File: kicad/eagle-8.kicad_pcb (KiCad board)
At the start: 4 copper layers, 127.1 x 96.7 mm, 33 parts, among them J1 SC242, J2 PGA387

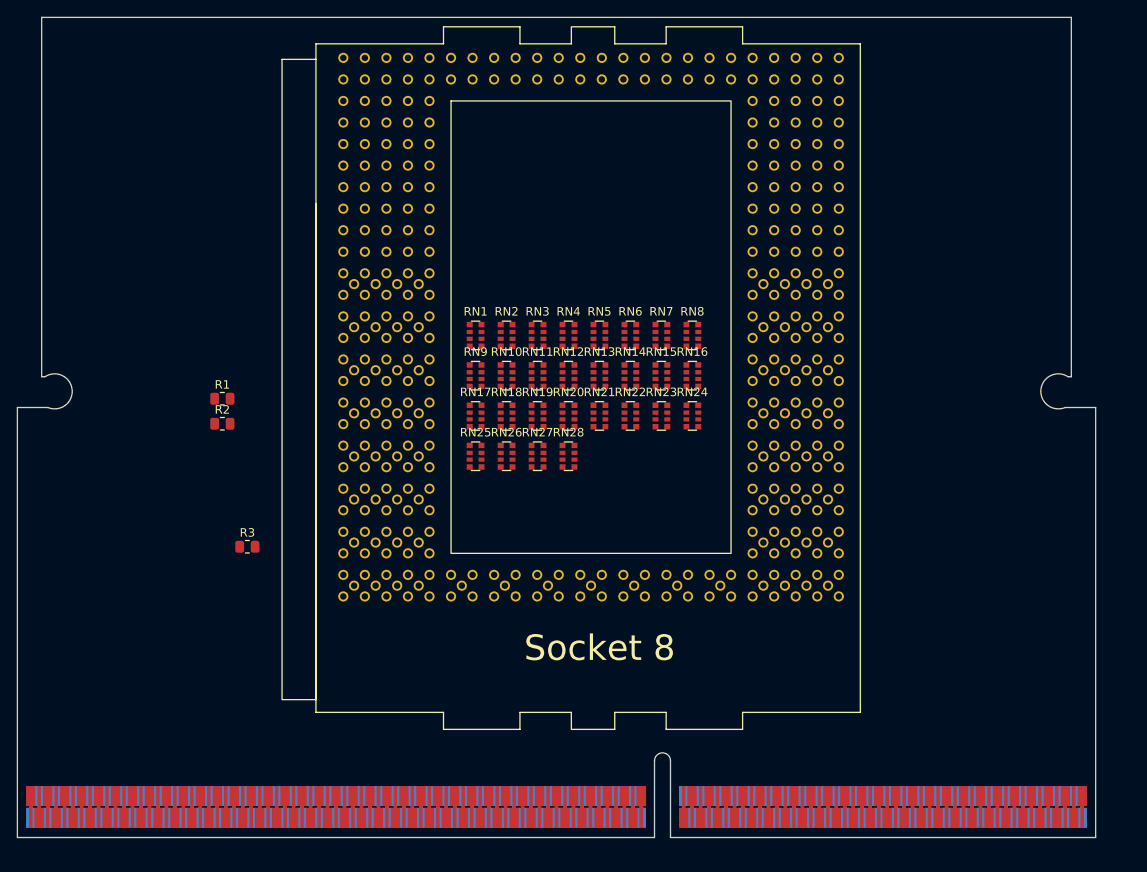
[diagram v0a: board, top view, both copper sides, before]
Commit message: fixed s8 footprint, important routing
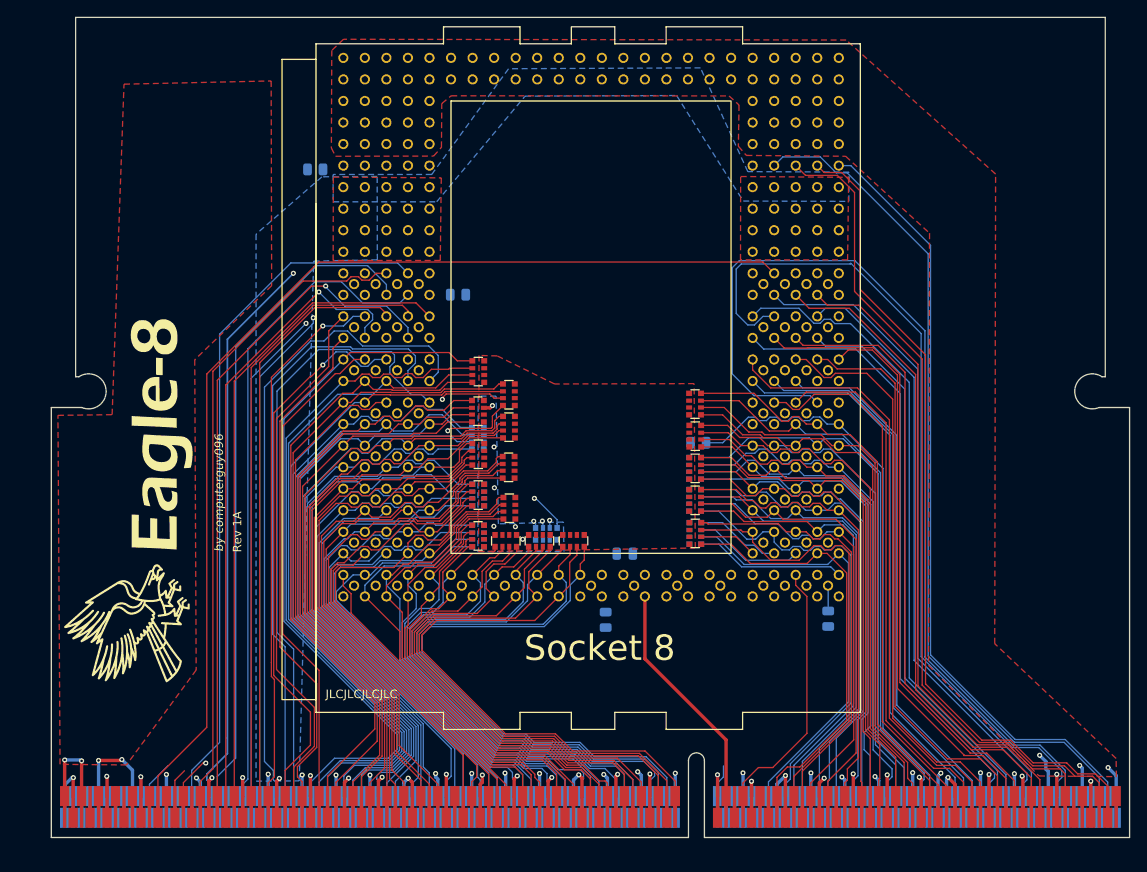
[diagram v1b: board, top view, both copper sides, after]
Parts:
- removed RN25, RN26, RN27, RN28: 56R, Resistor_SMD:R_Array_Convex_4x0612
- added C1: 100n, Capacitor_SMD:C_0805_2012Metric, B.Cu at (159.2, 98.5)
- added G***: LOGO, eagle-8:eagle-8, F.Cu at (104.6, 84.5)
- added R4: 0, Resistor_SMD:R_0805_2012Metric, B.Cu at (183.2, 106.1)
- added R5: 56R, Resistor_SMD:R_0805_2012Metric, B.Cu at (167.9, 85.4)
- added REF**: Logo, eagle-8:Logo, F.Cu at (101.3, 106.3)
- R1, R2: value 10K -> 1K; moved to B.Cu
- R3: value 150R -> 150R?; moved to B.Cu
- RN14, RN16, RN17, RN19, RN24, RN4, RN6: moved to B.Cu
- moved R3 43.1 mm to (157.0, 106.2), turned to 90 degrees
- moved R2 31.9 mm to (122.7, 53.1), turned to 180 degrees
- moved R1 30.4 mm to (139.6, 67.9), turned to 180 degrees
- moved RN8 28.0 mm to (153.2, 96.9), turned to 90 degrees
- moved RN1 27.1 mm to (167.5, 80.8), turned to 180 degrees
- moved RN14 26.1 mm to (141.9, 96.4)
- moved RN16 25.4 mm to (150.0, 96.1), turned to 90 degrees
- moved RN2 25.2 mm to (167.5, 84.6), turned to 180 degrees
- moved RN3 24.3 mm to (167.5, 88.4), turned to 180 degrees
- moved RN7 23.7 mm to (167.5, 96.1), turned to 180 degrees
- moved RN5 22.5 mm to (167.5, 92.2), turned to 180 degrees
- moved RN23 22.2 mm to (141.9, 77.0), turned to 180 degrees
- moved RN4 21.6 mm to (167.5, 88.4), turned to 180 degrees
- moved RN15 21.0 mm to (145.5, 88.3), turned to 180 degrees
- moved RN6 20.9 mm to (167.5, 92.2), turned to 180 degrees
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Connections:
- net /_BSEL0 renamed /BSEL0
- net /_BSEL1 renamed /BSEL1
- net /_SLP renamed /SLP
- J1 pad A1: VCC_VTT -> VTT
- J1 pad A11: /_TDO -> /TDO
- J1 pad A12: unconnected-(J1D-PWRGOOD-PadA12) -> /PGD
- J1 pad A15: /_THTRIP -> /THTRIP
- J1 pad A17: /_INTR -> /INTR
- J1 pad A19: /_PICD0 -> /PICD0
- J1 pad A20: /_PREQ -> /PREQ
- J1 pad A25: unconnected-(J1C-DEP#[0]-PadA25) -> /DEP0
- J1 pad A27: unconnected-(J1C-DEP#[1]-PadA27) -> /DEP1
- J1 pad A28: unconnected-(J1C-DEP#[3]-PadA28) -> /DEP3
- J1 pad A29: unconnected-(J1C-DEP#[5]-PadA29) -> /DEP5
- J1 pad A3: VCC_VTT -> VTT
- J1 pad A31: unconnected-(J1C-DEP#[6]-PadA31) -> /DEP6
- J1 pad A4: /_IERR -> /IERR
- J1 pad A5: /_A20M -> /A20M
- J1 pad A7: /_FERR -> /FERR
- J1 pad A76: unconnected-(J1C-BR0#-PadA76) -> /BR0
- J1 pad A79: unconnected-(J1A-A#[33]-PadA79) -> /A33
- J1 pad A8: /_IGNNE -> /IGNNE
- J1 pad A80: unconnected-(J1A-A#[34]-PadA80) -> /A34
- J1 pad A9: /_TDI -> /TDI
- J1 pad B1: GND -> unconnected-(J1C-EMI-PadB1)
- J1 pad B10: /_TMS -> /TMS
- J1 pad B100: GND -> unconnected-(J1C-EMI-PadB100)
- J1 pad B105: VCC_CORE -> Vcore
- J1 pad B11: /_TRST -> /TRST
- J1 pad B113: VCC_L2 -> VccL2
- J1 pad B117: VCC_L2 -> VccL2
- J1 pad B118: unconnected-(J1C-AERR#-PadB118) -> /AERR
- J1 pad B121: VCC_L2 -> VccL2
- J1 pad B13: VCC_CORE -> Vcore
- J1 pad B16: /_NMI -> /NMI
- J1 pad B17: VCC_CORE -> Vcore
- J1 pad B2: /_FLUSH -> /FLUSH
- J1 pad B22: /_PICD1 -> /PICD1
- J1 pad B25: VCC_CORE -> Vcore
- J1 pad B26: unconnected-(J1C-DEP#[2]-PadB26) -> /DEP2
- J1 pad B27: unconnected-(J1C-DEP#[4]-PadB27) -> /DEP4
- J1 pad B28: unconnected-(J1C-DEP#[7]-PadB28) -> /DEP7
- J1 pad B29: VCC_CORE -> Vcore
- J1 pad B3: /_SMI -> /SMI
- J1 pad B33: VCC_CORE -> Vcore
- J1 pad B37: VCC_CORE -> Vcore
- J1 pad B4: /_INIT -> /INIT
- J1 pad B41: GND -> unconnected-(J1C-EMI-PadB41)
- J1 pad B45: VCC_CORE -> Vcore
- J1 pad B49: VCC_CORE -> Vcore
- J1 pad B5: VCC_VTT -> VTT
- J1 pad B53: VCC_CORE -> Vcore
- J1 pad B57: VCC_CORE -> Vcore
- J1 pad B6: /_STPCLK -> /STPCLK
- J1 pad B61: GND -> unconnected-(J1C-EMI-PadB61)
- J1 pad B65: VCC_CORE -> Vcore
- J1 pad B69: VCC_CORE -> Vcore
- J1 pad B7: /_TCK -> /TCK
- J1 pad B73: VCC_CORE -> Vcore
- J1 pad B74: /_RESET -> /RESET
- J1 pad B75: unconnected-(J1C-BR1#-PadB75) -> /BR1
- J1 pad B77: VCC_CORE -> Vcore
- J1 pad B78: unconnected-(J1A-A#[35]-PadB78) -> /A35
- J1 pad B79: unconnected-(J1A-A#[32]-PadB79) -> /A32
- J1 pad B81: GND -> unconnected-(J1C-EMI-PadB81)
- J1 pad B85: VCC_CORE -> Vcore
- J1 pad B89: VCC_CORE -> Vcore
- J1 pad B9: VCC_VTT -> VTT
- J1 pad B93: VCC_CORE -> Vcore
- J1 pad B97: VCC_CORE -> Vcore
- J2 pad AA47: unconnected-(J2C-DEP#[5]-PadAA47) -> /DEP5
- J2 pad AB4: VccP -> Vcore
- J2 pad AB44: VccP -> Vcore
- J2 pad AC45: unconnected-(J2C-DEP#[0]-PadAC45) -> /DEP0
- J2 pad AC47: unconnected-(J2C-DEP#[3]-PadAC47) -> /DEP3
- J2 pad AC5: unconnected-(J2C-BR0#-PadAC5) -> /BR0
- J2 pad AE9: unconnected-(J2C-AERR#-PadAE9) -> /AERR
- J2 pad AG7: unconnected-(J2D-PWRGOOD-PadAG7) -> /PGD
- J2 pad AJ3: VccP -> Vcore
- J2 pad AJ41: VccP -> Vcore
- J2 pad AJ45: VccP -> Vcore
- J2 pad AJ7: VccP -> Vcore
- J2 pad AL1: VccP -> Vcore
- J2 pad AL39: VccP -> Vcore
- J2 pad AL43: VccP -> Vcore
- J2 pad AL47: VccP -> Vcore
- J2 pad AL5: VccP -> Vcore
- J2 pad AL9: VccP -> Vcore
- J2 pad AN3: VccP -> Vcore
- J2 pad AN41: VccP -> Vcore
- J2 pad AN45: VccP -> Vcore
- J2 pad AN7: VccP -> Vcore
- J2 pad AQ1: VccP -> Vcore
- J2 pad AQ39: VccP -> Vcore
- J2 pad AQ43: VccP -> Vcore
- J2 pad AQ47: VccP -> Vcore
- J2 pad AQ5: VccP -> Vcore
- J2 pad AQ9: VccP -> Vcore
- J2 pad AU1: Net-(J2D-VCC_CORE-PadAD32) -> VccL2
- J2 pad AU39: Net-(J2D-VCC_CORE-PadAD32) -> VccL2
- J2 pad AU43: Net-(J2D-VCC_CORE-PadAD32) -> VccL2
- J2 pad AU47: Net-(J2D-VCC_CORE-PadAD32) -> VccL2
- J2 pad AU5: Net-(J2D-VCC_CORE-PadAD32) -> VccL2
- J2 pad AU9: Net-(J2D-VCC_CORE-PadAD32) -> VccL2
- J2 pad AW3: Net-(J2D-VCC_CORE-PadAD32) -> VccL2
- J2 pad AW41: Net-(J2D-VCC_CORE-PadAD32) -> VccL2
- J2 pad AW45: Net-(J2D-VCC_CORE-PadAD32) -> VccL2
- J2 pad AW7: Net-(J2D-VCC_CORE-PadAD32) -> VccL2
- J2 pad AY1: Net-(J2D-VCC_CORE-PadAD32) -> VccL2
- J2 pad AY3: Net-(J2D-VCC_CORE-PadAD32) -> VccL2
- J2 pad AY39: Net-(J2D-VCC_CORE-PadAD32) -> VccL2
- J2 pad AY41: Net-(J2D-VCC_CORE-PadAD32) -> VccL2
- J2 pad AY43: Net-(J2D-VCC_CORE-PadAD32) -> VccL2
- J2 pad AY45: Net-(J2D-VCC_CORE-PadAD32) -> VccL2
- J2 pad AY47: Net-(J2D-VCC_CORE-PadAD32) -> VccL2
- J2 pad AY5: Net-(J2D-VCC_CORE-PadAD32) -> VccL2
- J2 pad AY7: Net-(J2D-VCC_CORE-PadAD32) -> VccL2
- J2 pad AY9: Net-(J2D-VCC_CORE-PadAD32) -> VccL2
- J2 pad B16: VccP -> Vcore
- J2 pad B24: VccP -> Vcore
- J2 pad B32: VccP -> Vcore
- J2 pad B4: VccP -> Vcore
- J2 pad B40: VccP -> Vcore
- J2 pad B44: VccP -> Vcore
- J2 pad B8: VccP -> Vcore
- J2 pad BA17: VccP -> Vcore
- J2 pad BA21: VccP -> Vcore
- J2 pad BA25: VccP -> Vcore
- J2 pad BA29: VccP -> Vcore
- J2 pad BA3: Net-(J2D-VCC_CORE-PadAD32) -> VccL2
- J2 pad BA41: Net-(J2D-VCC_CORE-PadAD32) -> VccL2
- J2 pad BA45: Net-(J2D-VCC_CORE-PadAD32) -> VccL2
- J2 pad BA7: Net-(J2D-VCC_CORE-PadAD32) -> VccL2
- J2 pad BC19: Net-(J2D-VCC_CORE-PadAD32) -> VccL2
- J2 pad BC23: Net-(J2D-VCC_CORE-PadAD32) -> VccL2
- J2 pad BC27: Net-(J2D-VCC_CORE-PadAD32) -> VccL2
- J2 pad BC31: Net-(J2D-VCC_CORE-PadAD32) -> VccL2
- J2 pad C1: unconnected-(J2A-A35-PadC1) -> /A35
- J2 pad C19: unconnected-(J2C-PLL1-PadC19) -> Net-(J2C-PLL1)
- J2 pad C23: unconnected-(J2C-PLL2-PadC23) -> Net-(J2C-PLL2)
- J2 pad E5: unconnected-(J2A-A32-PadE5) -> /A32
- J2 pad E7: unconnected-(J2A-A33-PadE7) -> /A33
- J2 pad E9: unconnected-(J2A-A34-PadE9) -> /A34
- J2 pad F2: VccP -> Vcore
- J2 pad F42: VccP -> Vcore
- J2 pad F46: VccP -> Vcore
- J2 pad F6: VccP -> Vcore
- J2 pad K4: VccP -> Vcore
- J2 pad K44: VccP -> Vcore
- J2 pad P2: VccP -> Vcore
- J2 pad P42: VccP -> Vcore
- J2 pad P46: VccP -> Vcore
- J2 pad P6: VccP -> Vcore
- J2 pad T4: VccP -> Vcore
- J2 pad T44: VccP -> Vcore
- J2 pad U39: unconnected-(J2C-DEP#[7]-PadU39) -> /DEP7
- J2 pad W3: unconnected-(J2C-BR1#-PadW3) -> /BR1
- J2 pad W39: unconnected-(J2C-DEP#[2]-PadW39) -> /DEP2
- J2 pad W41: unconnected-(J2C-DEP#[4]-PadW41) -> /DEP4
- J2 pad X42: VccP -> Vcore
- J2 pad X6: VccP -> Vcore
- J2 pad Y43: unconnected-(J2C-DEP#[1]-PadY43) -> /DEP1
- J2 pad Y45: unconnected-(J2C-DEP#[6]-PadY45) -> /DEP6
- R1 pad 1: VccP -> Vcore
- RN1 pad 1: /A3 -> /A5
- RN1 pad 2: /A4 -> /A9
- RN1 pad 3: /A5 -> /A3
- RN1 pad 4: /A6 -> /A4
- RN10 pad 1: /D8 -> /D15
- RN10 pad 2: /D9 -> /D12
- RN10 pad 3: /D10 -> /D9
- RN10 pad 4: /D11 -> /D8
- RN11 pad 1: /D12 -> /D11
- RN11 pad 2: /D13 -> /D17
- RN11 pad 3: /D14 -> /D10
- RN11 pad 4: /D15 -> /D14
- RN12 pad 1: /D16 -> /D28
- RN12 pad 2: /D17 -> /D30
- RN12 pad 3: /D18 -> /D27
- RN12 pad 4: /D19 -> /D23
- RN13 pad 1: /D20 -> /D18
- RN13 pad 2: /D21 -> /D22
- RN13 pad 3: /D22 -> /D13
- RN13 pad 4: /D23 -> /D20
- RN14 pad 1: /D24 -> /D16
- RN14 pad 2: /D25 -> /D19
- RN14 pad 4: /D27 -> /D29
- RN15 pad 5: unconnected-(RN15-R4.2-Pad5) -> /D37
- RN15 pad 6: unconnected-(RN15-R3.2-Pad6) -> /D33
- RN15 pad 7: unconnected-(RN15-R2.2-Pad7) -> /D32
- RN15 pad 8: unconnected-(RN15-R1.2-Pad8) -> /D35
- RN16 pad 5: unconnected-(RN16-R4.2-Pad5) -> /D21
- RN16 pad 6: unconnected-(RN16-R3.2-Pad6) -> /D24
- RN16 pad 7: unconnected-(RN16-R2.2-Pad7) -> /D25
- RN16 pad 8: unconnected-(RN16-R1.2-Pad8) -> /D38
- RN17 pad 5: unconnected-(RN17-R4.2-Pad5) -> /D31
- RN17 pad 6: unconnected-(RN17-R3.2-Pad6) -> /D34
- RN17 pad 7: unconnected-(RN17-R2.2-Pad7) -> /D36
- RN17 pad 8: unconnected-(RN17-R1.2-Pad8) -> /D47
- RN18 pad 5: unconnected-(RN18-R4.2-Pad5) -> /D44
- RN18 pad 6: unconnected-(RN18-R3.2-Pad6) -> /D39
- RN18 pad 7: unconnected-(RN18-R2.2-Pad7) -> /D43
- RN18 pad 8: unconnected-(RN18-R1.2-Pad8) -> /D40
- RN19 pad 5: unconnected-(RN19-R4.2-Pad5) -> /D41
- RN19 pad 6: unconnected-(RN19-R3.2-Pad6) -> /D48
- RN19 pad 7: unconnected-(RN19-R2.2-Pad7) -> /D54
- RN19 pad 8: unconnected-(RN19-R1.2-Pad8) -> /D50
- RN2 pad 1: /A7 -> /A17
- RN2 pad 2: /A8 -> /A14
- RN2 pad 3: /A9 -> /A10
- RN2 pad 4: /A10 -> /A8
- RN20 pad 5: /D60 -> /D49
- RN20 pad 6: /D61 -> /D52
- RN20 pad 7: /D62 -> /D51
- RN20 pad 8: /D63 -> /D45
- RN21 pad 5: /D56 -> /D55
- RN21 pad 6: /D57 -> /D56
- RN21 pad 7: /D58 -> /D60
- RN21 pad 8: /D59 -> /D42
- RN22 pad 5: /D52 -> /D53
- RN22 pad 6: /D53 -> /D57
- RN22 pad 7: /D54 -> /D59
- RN22 pad 8: /D55 -> /D46
- RN23 pad 5: /D48 -> /D62
- RN23 pad 6: /D49 -> /D58
- RN23 pad 7: /D50 -> /D63
- RN23 pad 8: /D51 -> /D61
- RN24 pad 1: VTT -> /A33
- RN24 pad 2: VTT -> /A32
- RN24 pad 3: VTT -> /A29
- RN24 pad 4: VTT -> /A35
- RN24 pad 5: /D44 -> VTT
- RN24 pad 6: /D45 -> VTT
- RN24 pad 7: /D46 -> VTT
- RN24 pad 8: /D47 -> VTT
- RN3 pad 1: /A11 -> /A18
- RN3 pad 2: /A12 -> /A25
- RN3 pad 3: /A13 -> /A16
- RN3 pad 4: /A14 -> /A13
- RN4 pad 1: /A15 -> /A7
- RN4 pad 2: /A16 -> /A12
- RN4 pad 3: /A17 -> /A11
- RN4 pad 4: /A18 -> /A15
- RN5 pad 1: /A19 -> /A24
- RN5 pad 2: /A20 -> /A23
- RN5 pad 3: /A21 -> /A28
- RN5 pad 4: /A22 -> /A19
- RN6 pad 1: /A23 -> /A21
- RN6 pad 2: /A24 -> /A20
- RN6 pad 3: /A25 -> /A22
- RN7 pad 1: /A27 -> /A30
- RN7 pad 2: /A28 -> /A34
- RN7 pad 3: /A29 -> /A31
- RN7 pad 4: /A30 -> /A27
- RN8 pad 1: /D0 -> /D4
- RN8 pad 2: /D1 -> /D2
- RN8 pad 3: /D2 -> /D1
- RN8 pad 4: /D3 -> /D0
- RN9 pad 1: /D4 -> /D7
- RN9 pad 2: /D5 -> /D6
- RN9 pad 3: /D6 -> /D5
- RN9 pad 4: /D7 -> /D3
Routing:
- net Vcore: track 0.00 -> 213.3 mm, vias 0 -> 19
- net /PGD: track 0.00 -> 125.2 mm
- net /RSP: track 0.00 -> 114.1 mm
- net /RP: track 0.00 -> 99.7 mm
- net /VID3: track 0.00 -> 99.1 mm
- net /VID2: track 0.00 -> 96.8 mm
- net /VID1: track 0.00 -> 95.4 mm
- net /VID0: track 0.00 -> 91.7 mm
- net GND: track 0.00 -> 85.7 mm, vias 0 -> 29
- net /D62: track 0.00 -> 83.8 mm
- net /NMI: track 0.00 -> 82.0 mm
- net /D58: track 0.00 -> 81.6 mm
- net /PICCLK: track 0.00 -> 81.4 mm, vias 0 -> 1
- net /D63: track 0.00 -> 79.8 mm
- net /PICD0: track 0.00 -> 79.4 mm, vias 0 -> 1
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- added copper zone on In1.Cu, net GND
- added copper zone on In2.Cu, net GND
- added copper zone on B.Cu, net VTT
- added copper zone on F.Cu, net VTT
- added copper zone on F.Cu, net VccL2
- added copper zone on B.Cu, net Vcore
- added copper zone on F.Cu, net Vcore
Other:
- board text added: "Designed in Romania"
- board text added: "JLCJLCJLCJLC"
- board text added: "Rev 1A"
- board text added: "by computerguy096"

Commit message: finished routing, added AM3 mounting holes
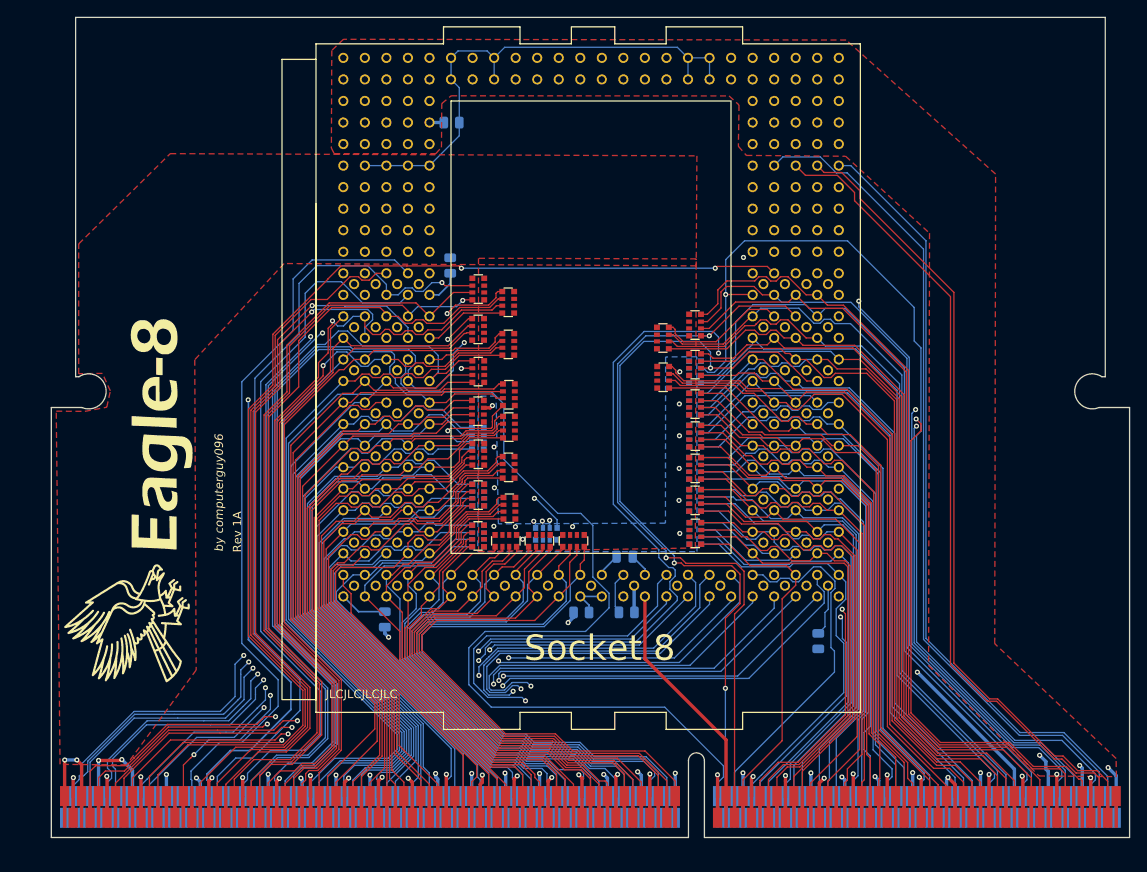
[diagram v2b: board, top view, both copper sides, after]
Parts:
- removed R5: 56R, Resistor_SMD:R_0805_2012Metric
- added R7: 1K, Resistor_SMD:R_0805_2012Metric, B.Cu at (159.4, 105.4)
- added R8: 1K, Resistor_SMD:R_0805_2012Metric, B.Cu at (138.8, 47.6)
- added RN25: 56R, Resistor_SMD:R_Array_Convex_4x0612, F.Cu at (141.9, 72.0)
- added RN26: 56R, Resistor_SMD:R_Array_Convex_4x0612, F.Cu at (145.5, 73.8)
- added RN27: 56R, Resistor_SMD:R_Array_Convex_4x0612, B.Cu at (167.5, 80.8)
- added RN28: 56R, Resistor_SMD:R_Array_Convex_4x0612, F.Cu at (141.9, 67.2)
- added RN29: 56R, Resistor_SMD:R_Array_Convex_4x0612, F.Cu at (167.5, 71.5)
- added RN30: 56R, Resistor_SMD:R_Array_Convex_4x0612, B.Cu at (167.5, 77.0)
- added RN31: 56R, Resistor_SMD:R_Array_Convex_4x0612, F.Cu at (163.8, 77.7)
- added RN32: 56R, Resistor_SMD:R_Array_Convex_4x0612, F.Cu at (145.5, 68.8)
- added RN33: 56R, Resistor_SMD:R_Array_Convex_4x0612, F.Cu at (163.7, 73.0)
- added RN34: 56R, Resistor_SMD:R_Array_Convex_4x0612, F.Cu at (167.5, 76.2)
- added RN35: 56R, Resistor_SMD:R_Array_Convex_4x0612, B.Cu at (167.5, 84.6)
- moved R2 60.9 mm to (154.1, 105.4)
- moved R3 26.0 mm to (130.9, 106.2), turned to -90 degrees
- moved R1 3.56 mm to (138.6, 64.5), turned to -90 degrees
- moved R4 2.89 mm to (182.0, 108.8)
- moved C1 0.36 mm to (159.2, 98.8)
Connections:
- J1 pad A117: unconnected-(J1A-AP#[0]-PadA117) -> /AP0
- J1 pad A14: /BSEL1 -> unconnected-(J1C-BSEL1-PadA14)
- J1 pad B116: unconnected-(J1A-AP#[1]-PadB116) -> /AP1
- J1 pad B21: /BSEL0 -> unconnected-(J1C-BSEL0-PadB21)
- J1 pad B8: /SLP -> unconnected-(J1C-SLP#-PadB8)
- J2 pad AE39: Net-(J2D-TESTHI-PadA23) -> Net-(J2D-TESTHI-PadAE39)
- J2 pad B2: unconnected-(J2C-CPUPRES#-PadB2) -> Net-(J2C-CPUPRES#)
- J2 pad C21: Net-(J2D-TESTLO-PadAS39) -> Net-(J2D-TESTLO-PadC21)
- J2 pad S9: unconnected-(J2A-AP1-PadS9) -> /AP1
- J2 pad U1: unconnected-(J2A-AP0-PadU1) -> /AP0
- R1 pad 2: Net-(J2D-TESTHI-PadA23) -> Net-(J2D-TESTHI-PadAE39)
- R2 pad 1: Net-(J2D-TESTLO-PadAS39) -> Net-(J2D-TESTHI-PadA23)
- R2 pad 2: GND -> Vcore
- R4 pad 1: unconnected-(J2C-CPUPRES#-PadB2) -> Net-(J2C-CPUPRES#)
- RN1 pad 1: /A5 -> /A8
- RN1 pad 2: /A9 -> /A5
- RN1 pad 3: /A3 -> /A9
- RN1 pad 4: /A4 -> /AP1
- RN2 pad 1: /A17 -> /A13
- RN2 pad 2: /A14 -> /A17
- RN2 pad 3: /A10 -> /A14
- RN2 pad 4: /A8 -> /A10
- RN21 pad 7: /D60 -> /DEP7
- RN23 pad 5: /D62 -> /DEP2
- RN23 pad 6: /D58 -> /D60
- RN3 pad 1: /A18 -> /A19
- RN3 pad 2: /A25 -> /A18
- RN3 pad 3: /A16 -> /A25
- RN3 pad 4: /A13 -> /A16
- RN5 pad 1: /A24 -> /A27
- RN5 pad 2: /A23 -> /A24
- RN5 pad 3: /A28 -> /A23
- RN5 pad 4: /A19 -> /A28
- RN7 pad 1: /A30 -> /BERR
- RN7 pad 3: /A31 -> /A30
- RN7 pad 4: /A27 -> /A31
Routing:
- net Net-(J2D-VREF0): track 0.00 -> 160.8 mm
- net Vcore: track 213.3 -> 53.3 mm, vias 19 -> 20
- net /SMI: track 0.00 -> 148.3 mm, vias 0 -> 3
- net /RESET: track 3.85 -> 126.5 mm, vias 0 -> 1
- net /AERR: track 0.00 -> 115.6 mm, vias 0 -> 1
- net /IERR: track 0.00 -> 105.1 mm, vias 0 -> 2
- net /IGNNE: track 0.00 -> 102.1 mm, vias 0 -> 2
- net /STPCLK: track 0.00 -> 98.9 mm, vias 0 -> 2
- net /FERR: track 0.00 -> 97.8 mm, vias 0 -> 2
- net /TCK: track 0.00 -> 95.9 mm, vias 0 -> 2
- net /TDI: track 0.00 -> 95.4 mm, vias 0 -> 2
- net /INIT: track 0.00 -> 94.2 mm, vias 0 -> 2
- net /TDO: track 0.00 -> 94.1 mm, vias 0 -> 2
- net /A20M: track 0.00 -> 91.7 mm, vias 0 -> 2
- net /BR1: track 0.00 -> 91.4 mm, vias 0 -> 3
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- added copper zone on In2.Cu, net Vcore
- removed copper zone on In2.Cu, net GND
- removed copper zone on B.Cu, net Vcore
- removed copper zone on F.Cu, net Vcore

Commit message: more improvements
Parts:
- removed R4: 0, Resistor_SMD:R_0805_2012Metric
- removed R7, R8: 1K, Resistor_SMD:R_0805_2012Metric
- added C10: 100n, Capacitor_SMD:C_0805_2012Metric, F.Cu at (164.0, 82.2)
- added C11: 100n, Capacitor_SMD:C_0805_2012Metric, F.Cu at (164.5, 68.9)
- added C12: 100n, Capacitor_SMD:C_0805_2012Metric, F.Cu at (157.8, 96.4)
- added C13: 100n, Capacitor_SMD:C_0805_2012Metric, F.Cu at (163.7, 96.0)
- added C14: 100n, Capacitor_SMD:C_0805_2012Metric, B.Cu at (158.6, 47.8)
- added C15: 100n, Capacitor_SMD:C_0805_2012Metric, B.Cu at (154.4, 47.8)
- added C16: 100n, Capacitor_SMD:C_0805_2012Metric, B.Cu at (150.2, 47.9)
- added C17: 100n, Capacitor_SMD:C_0805_2012Metric, B.Cu at (152.3, 47.9)
- added C18: 100n, Capacitor_SMD:C_0805_2012Metric, B.Cu at (160.7, 47.8)
- added C19: 100n, Capacitor_SMD:C_0805_2012Metric, B.Cu at (146.0, 47.9)
- added C2: 100n, Capacitor_SMD:C_0805_2012Metric, F.Cu at (149.1, 69.3)
- added C20: 100n, Capacitor_SMD:C_0805_2012Metric, B.Cu at (156.5, 47.8)
- added C21: 100n, Capacitor_SMD:C_0805_2012Metric, B.Cu at (148.1, 47.9)
- added C22: 100n, Capacitor_SMD:C_0805_2012Metric, B.Cu at (162.8, 47.8)
- added C23: 100n, Capacitor_SMD:C_0805_2012Metric, B.Cu at (164.8, 47.8)
- added C24: 100n, Capacitor_SMD:C_0805_2012Metric, F.Cu at (152.4, 47.9)
- added C25: 100n, Capacitor_SMD:C_0805_2012Metric, F.Cu at (158.6, 47.8)
- added C26: 100n, Capacitor_SMD:C_0805_2012Metric, F.Cu at (160.7, 47.8)
- added C27: 100n, Capacitor_SMD:C_0805_2012Metric, F.Cu at (150.2, 47.9)
- added C28: 100n, Capacitor_SMD:C_0805_2012Metric, F.Cu at (154.4, 47.8)
- added C29: 100n, Capacitor_SMD:C_0805_2012Metric, F.Cu at (156.5, 47.8)
- added C3: 100n, Capacitor_SMD:C_0805_2012Metric, F.Cu at (148.6, 76.8)
- added C30: 47uF, Capacitor_Tantalum_SMD:CP_EIA-7343-40_Kemet-Y_HandSolder, F.Cu at (160.3, 55.7)
- added C31: 47uF, Capacitor_Tantalum_SMD:CP_EIA-7343-40_Kemet-Y_HandSolder, F.Cu at (151.6, 55.7)
- added C32: 47uF, Capacitor_Tantalum_SMD:CP_EIA-7343-40_Kemet-Y_HandSolder, B.Cu at (146.8, 55.2)
- added C33: 47uF, Capacitor_Tantalum_SMD:CP_EIA-7343-40_Kemet-Y_HandSolder, B.Cu at (152.6, 55.2)
- added C34: 47uF, Capacitor_Tantalum_SMD:CP_EIA-7343-40_Kemet-Y_HandSolder, B.Cu at (158.5, 55.2)
- added C35: 47uF, Capacitor_Tantalum_SMD:CP_EIA-7343-40_Kemet-Y_HandSolder, B.Cu at (164.3, 55.2)
- added C36: 47uF, Capacitor_Tantalum_SMD:CP_EIA-7343-40_Kemet-Y_HandSolder, F.Cu at (208.3, 68.5)
- added C37: 47uF, Capacitor_Tantalum_SMD:CP_EIA-7343-40_Kemet-Y_HandSolder, F.Cu at (208.3, 79.0)
- added C4: 100n, Capacitor_SMD:C_0805_2012Metric, F.Cu at (148.8, 83.9)
- added C5: 100n, Capacitor_SMD:C_0805_2012Metric, F.Cu at (149.0, 90.5)
- added C6: 100n, Capacitor_SMD:C_0805_2012Metric, F.Cu at (151.6, 93.7)
- added C7: 100n, Capacitor_SMD:C_0805_2012Metric, F.Cu at (163.6, 92.2)
- added C8: 100n, Capacitor_SMD:C_0805_2012Metric, F.Cu at (163.5, 88.4)
- added C9: 100n, Capacitor_SMD:C_0805_2012Metric, F.Cu at (163.6, 85.0)
- added CN1: AM3 bracket, eagle-8:AM3 bracket, F.Cu at (153.3, 71.7)
- added H1: 6mm, MountingHole:MountingHole_6mm, F.Cu at (201.2, 47.7)
- added H2: 6mm, MountingHole:MountingHole_6mm, F.Cu at (201.2, 95.7)
- added H3: 6mm, MountingHole:MountingHole_6mm, F.Cu at (105.2, 47.7)
- added H4: 6mm, MountingHole:MountingHole_6mm, F.Cu at (105.2, 95.7)
- added J3: same as Vcore, Connector_PinHeader_2.54mm:PinHeader_2x04_P2.54mm_Vertical, F.Cu at (199.8, 106.3)
- added J4: Slot 1 L2, Connector_PinHeader_2.54mm:PinHeader_2x04_P2.54mm_Vertical, F.Cu at (206.0, 106.3)
- added R14: 56R, Resistor_SMD:R_0805_2012Metric, B.Cu at (167.9, 99.0)
- R1, R2: value 1K -> 150R; moved to F.Cu
- R3: value 150R? -> 150R
- moved R2 42.9 mm to (142.3, 64.2)
- moved REF** 23.0 mm to (110.7, 85.4)
- moved G*** 22.4 mm to (112.2, 63.4)
- moved RN16 5.31 mm to (145.6, 93.1), turned to 180 degrees
- moved R1 4.37 mm to (142.3, 62.1), turned to 180 degrees
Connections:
- J2 pad A23: Net-(J2D-TESTHI-PadA23) -> Vcore
- J2 pad A25: Net-(J2D-TESTHI-PadA23) -> Vcore
- J2 pad AA1: unconnected-(J2C-BR2#-PadAA1) -> /BR2
- J2 pad AE39: Net-(J2D-TESTHI-PadAE39) -> Vcore
- J2 pad AS39: Net-(J2D-TESTLO-PadAS39) -> GND
- J2 pad AS41: Net-(J2D-TESTLO-PadAS39) -> GND
- J2 pad AS43: Net-(J2D-TESTLO-PadAS39) -> GND
- J2 pad AS45: Net-(J2D-TESTLO-PadAS39) -> GND
- J2 pad AU1: VccL2 -> VccS
- J2 pad AU39: VccL2 -> VccS
- J2 pad AU43: VccL2 -> VccS
- J2 pad AU47: VccL2 -> VccS
- J2 pad AU5: VccL2 -> VccS
- J2 pad AU9: VccL2 -> VccS
- J2 pad AW3: VccL2 -> VccS
- J2 pad AW41: VccL2 -> VccS
- J2 pad AW45: VccL2 -> VccS
- J2 pad AW7: VccL2 -> VccS
- J2 pad AY1: VccL2 -> VccS
- J2 pad AY3: VccL2 -> VccS
- J2 pad AY39: VccL2 -> VccS
- J2 pad AY41: VccL2 -> VccS
- J2 pad AY43: VccL2 -> VccS
- J2 pad AY45: VccL2 -> VccS
- J2 pad AY47: VccL2 -> VccS
- J2 pad AY5: VccL2 -> VccS
- J2 pad AY7: VccL2 -> VccS
- J2 pad AY9: VccL2 -> VccS
- J2 pad B2: Net-(J2C-CPUPRES#) -> unconnected-(J2C-CPUPRES#-PadB2)
- J2 pad BA13: Net-(J2D-TESTLO-PadAS39) -> GND
- J2 pad BA15: Net-(J2D-TESTLO-PadAS39) -> GND
- J2 pad BA3: VccL2 -> VccS
- J2 pad BA33: Net-(J2D-TESTLO-PadAS39) -> GND
- J2 pad BA37: Net-(J2D-TESTLO-PadAS39) -> GND
- J2 pad BA41: VccL2 -> VccS
- J2 pad BA45: VccL2 -> VccS
- J2 pad BA7: VccL2 -> VccS
- J2 pad BC13: Net-(J2D-TESTLO-PadAS39) -> GND
- J2 pad BC15: Net-(J2D-TESTLO-PadAS39) -> GND
- J2 pad BC19: VccL2 -> VccS
- J2 pad BC23: VccL2 -> VccS
- J2 pad BC27: VccL2 -> VccS
- J2 pad BC31: VccL2 -> VccS
- J2 pad BC33: Net-(J2D-TESTLO-PadAS39) -> GND
- J2 pad BC37: Net-(J2D-TESTLO-PadAS39) -> GND
- J2 pad C21: Net-(J2D-TESTLO-PadC21) -> GND
- J2 pad U9: unconnected-(J2C-BR3#-PadU9) -> /BR3
- R1 pad 1: Vcore -> VTT
- R1 pad 2: Net-(J2D-TESTHI-PadAE39) -> Net-(J2D-VREF0)
- R2 pad 1: Net-(J2D-TESTHI-PadA23) -> VTT
- R2 pad 2: Vcore -> Net-(J2D-VREF0)
- RN10 pad 1: /D15 -> /D12
- RN10 pad 2: /D12 -> /D14
- RN11 pad 1: /D11 -> /D17
- RN11 pad 2: /D17 -> /D11
- RN11 pad 3: /D10 -> /D15
- RN11 pad 4: /D14 -> /D10
- RN12 pad 4: /D23 -> /D25
- RN13 pad 1: /D18 -> /D22
- RN13 pad 2: /D22 -> /D21
- RN13 pad 3: /D13 -> /D18
- RN13 pad 4: /D20 -> /D13
- RN14 pad 1: /D16 -> /D24
- RN14 pad 2: /D19 -> /D20
- RN14 pad 3: /D26 -> /D16
- RN14 pad 4: /D29 -> /D19
- RN16 pad 5: /D21 -> /D23
- RN16 pad 6: /D24 -> /D26
- RN16 pad 7: /D25 -> /D29
- RN16 pad 8: /D38 -> /D31
- RN17 pad 5: /D31 -> /D38
- RN27 pad 5: /REQ3 -> /REQ2
- RN27 pad 7: /REQ2 -> /REQ4
- RN27 pad 8: /REQ4 -> /REQ0
- RN28 pad 5: unconnected-(RN28-R4.2-Pad5) -> /AERR
- RN30 pad 5: unconnected-(RN30-R4.2-Pad5) -> /HIT
- RN30 pad 6: /AERR -> /BR2
- RN30 pad 7: /HIT -> /LOCK
- RN30 pad 8: /LOCK -> /REQ3
- RN35 pad 5: /REQ0 -> /RSP
- RN35 pad 6: /RSP -> /BR3
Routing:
- net Net-(J2D-TESTLO-PadAS39): track 62.0 -> 0.00 mm
- net GND: track 81.9 -> 123.6 mm, vias 30 -> 54
- net /AERR: track 115.6 -> 138.5 mm
- net /BR2: track 0.00 -> 21.2 mm
- net /PRDY: track 89.8 -> 110.6 mm, vias 1 -> 0
- net /D1: track 64.6 -> 53.8 mm
- net /IGNNE: track 102.1 -> 91.5 mm
- net /D5: track 59.8 -> 49.2 mm
- net /D3: track 62.5 -> 51.9 mm
- net /D38: track 70.9 -> 60.7 mm, vias 1 -> 0
- net /D24: track 67.9 -> 58.0 mm
- net /FERR: track 97.8 -> 88.3 mm
- net /D8: track 56.8 -> 47.4 mm
- net /TDI: track 95.4 -> 86.0 mm
- net /D25: track 68.4 -> 59.4 mm, vias 1 -> 0
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- added copper zone on B.Cu, net GND
- added copper zone on F.Cu, net GND
- added copper zone on F.Cu, net VccS
- added copper zone on B.Cu, net Vcore
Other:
- board size 127.1 x 96.7 mm -> 127.1 x 98.7 mm
- board text added: "Do NOT insert jumpers into both headers at the same time!"
- board text added: "L2 voltage"
